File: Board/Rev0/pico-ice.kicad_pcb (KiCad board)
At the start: 4 copper layers, 22.9 x 61 mm, 109 parts, among them J1 USB_C_Receptacle_USB2.0, J10 2x3_2.54mm_Female, J11 2x3_2.54mm_Female, J2 SWD, J3 6X2 Female Header, J4 6X2 Female Header, J6 6X2 Female Header, J7 6X2 Female Header, J8 6X2 Female Header, J9 BOOT_SEL, SW1 PTS820 J25K SMTR LFS, SW2 PTS820 J25K SMTR LFS, U1 NCP1117ST33T3G, U2 W25Q32JVSSIQ, U3 RP2040, U4 CL9293A12L5M, U5 APS6404L-3SQN-SN, U6 ICE40UP5K-SG48ITR, U8 W25Q32JVSSIQ, Y1 12 MHz

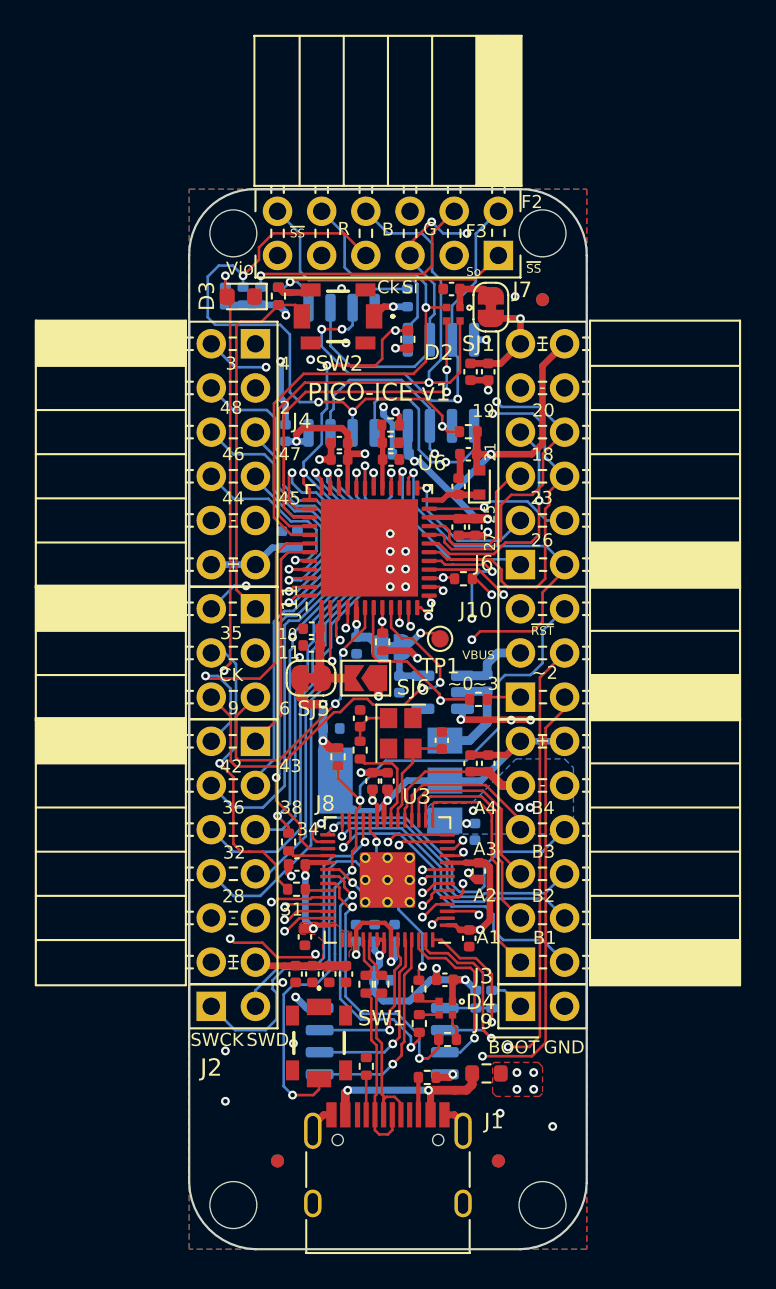
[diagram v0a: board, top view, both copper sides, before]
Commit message: Added block diagram and rendering files. Changed layers for logo and board name to be the mask layer
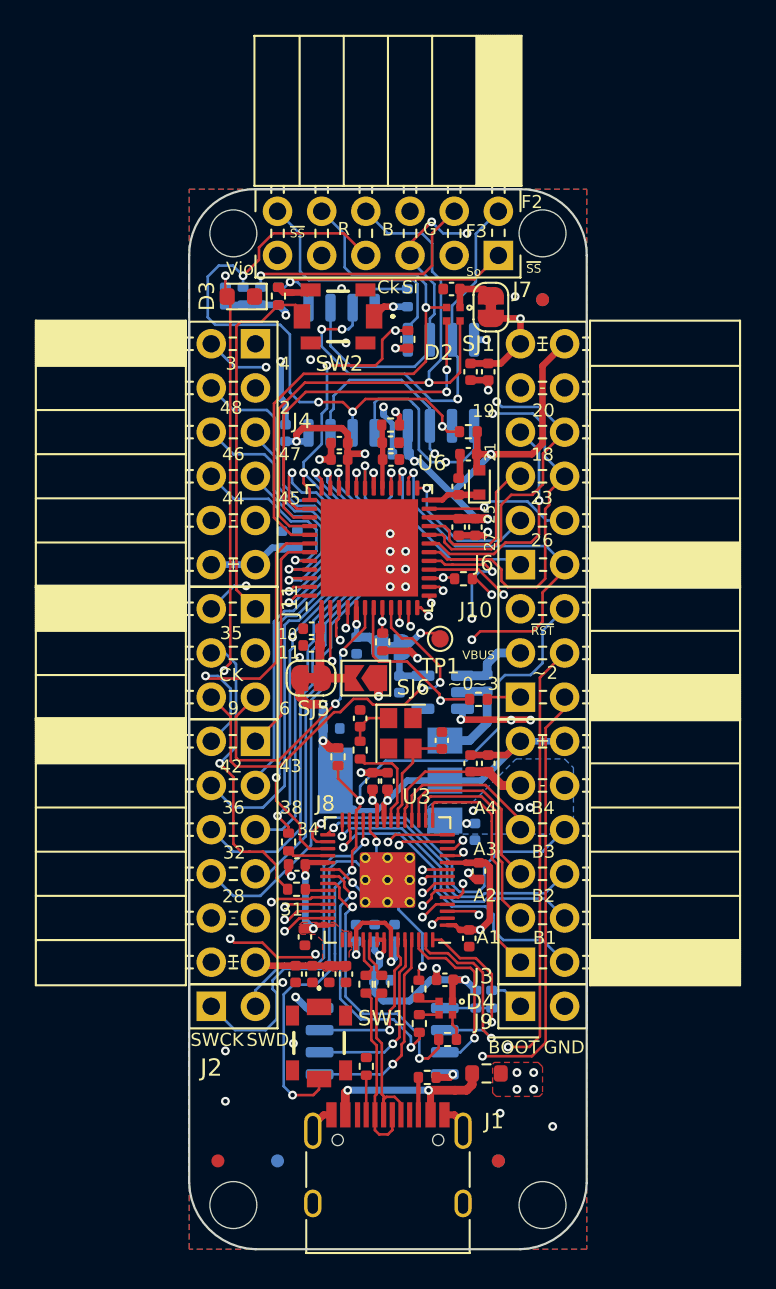
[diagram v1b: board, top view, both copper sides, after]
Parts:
- moved FID5 3.43 mm to (62.6, 129.5)
- moved LOGO1 2.48 mm to (63.4, 127.5), turned to 90 degrees
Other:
- board text added: "pico-ice v1"
- board text removed: "PICO-ICE v1"
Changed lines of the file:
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@@
   )
   (footprint "CUSTOM:tinyAI_logo" (layer "F.Cu")
-    (at 64.70144 125.408866)
+    (at 63.373 127.508 90)
     (property "Digi-Key_PN" "DNP")
     (property "MPN" "DNP")
@@
     (property "exclude_from_bom" "")
     (attr board_only exclude_from_pos_files exclude_from_bom)
-    (fp_text reference "LOGO1" (at 0 0) (layer "F.SilkS") hide
+    (fp_text reference "LOGO1" (at 0 0 90) (layer "F.SilkS") hide
       (effects (font (size 1.524 1.524) (thickness 0.3)))
     )
-    (fp_text value "tinyVS Logo" (at 0.75 0) (layer "F.SilkS") hide
+    (fp_text value "tinyVS Logo" (at 0.75 0 90) (layer "F.SilkS") hide
       (effects (font (size 1.524 1.524) (thickness 0.3)))
     )
@@
   )
   (footprint "Fiducial:Fiducial_0.75mm_Mask1.5mm" locked (layer "F.Cu")
-    (at 66.04 129.54)
+    (at 62.611 129.54)
     (descr "Circular Fiducial, 0.75mm bare copper, 1.5mm soldermask opening (Level B)")
     (tags "fiducial")
@@
     (effects (font (size 0.75 0.75) (thickness 0.12)) (justify mirror))
   )
-  (gr_text "PICO-ICE v1" (at 72.263 130.048) (layer "B.SilkS")
-    (effects (font (size 1.143 1.143) (thickness 0.254)) (justify mirror))
-  )
   (gr_text "A4" (at 78.6384 109.2454) (layer "B.SilkS")
     (effects (font (size 0.75 0.75) (thickness 0.12)) (justify mirror))
@@
     (effects (font (size 0.75 0.75) (thickness 0.1)))
   )
-  (gr_text "PICO-ICE v1" (at 71.882 85.344) (layer "F.SilkS")
-    (effects (font (size 1.016 1.016) (thickness 0.254)))
-  )
   (gr_text "B3" (at 81.3308 111.76) (layer "F.SilkS")
     (effects (font (size 0.75 0.75) (thickness 0.1)))
@@
     (effects (font (size 0.75 0.75) (thickness 0.1)))
   )
+  (gr_text "pico-ice v1" (at 72.39 129.921) (layer "B.Mask")
+    (effects (font (size 1.143 1.143) (thickness 0.254)) (justify mirror))
+  )
+  (gr_text "pico-ice v1" (at 65.405 127.635 90) (layer "F.Mask")
+    (effects (font (size 0.9 0.9) (thickness 0.125)))
+  )
   (segment (start 78.156 85.2168) (end 78.1558 85.217) (width 0.381) (layer "F.Cu") (net 1))
